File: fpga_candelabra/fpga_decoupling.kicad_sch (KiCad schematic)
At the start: 57 parts

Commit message: fpga_candelabra: more bugfixes & improvements for rev 0.2.0
- Add Digilent JTAG-SMT2-NC onboard
- Add fan controller & 4pin fan header
- Use 9pin header for USB2.0
- Misc fixes for structure

Signed-off-by: Yichuan Gao <gaoyichuan000@gmail.com>
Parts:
- C148, C149, C150, C151, C152, C153, C154, C155, C156, C157, C158: footprint Capacitor_SMD:C_1206_3216Metric -> Capacitor_Tantalum_SMD:CP_EIA-3528-21_Kemet-B; symbol Device:C_Small -> Device:C_Polarized_Small_US; LCSC Part (none) -> C171850
- C159, C166, C167, C168, C169: footprint Capacitor_SMD:C_1210_3225Metric -> Capacitor_Tantalum_SMD:CP_EIA-3528-21_Kemet-B; symbol Device:C_Small -> Device:C_Polarized_Small_US; LCSC Part (none) -> C696807

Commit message: fpga_candelabra: add author & rev to schematics
Signed-off-by: Yichuan Gao <gaoyichuan000@gmail.com>
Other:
- company: (none) -> CHIPS Alliance
- title: (none) -> FPGA Decoupling Capacitors
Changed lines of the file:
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@@
 	(generator_version "8.0")
 	(paper "A4")
+	(title_block
+		(title "FPGA Decoupling Capacitors")
+		(date "2025-02-05")
+		(rev "0.2.0")
+		(company "CHIPS Alliance")
+		(comment 1 "Yichuan Gao")
+		(comment 2 "Yichuan Gao")
+	)
 	(junction
 		(at 171.45 82.55)

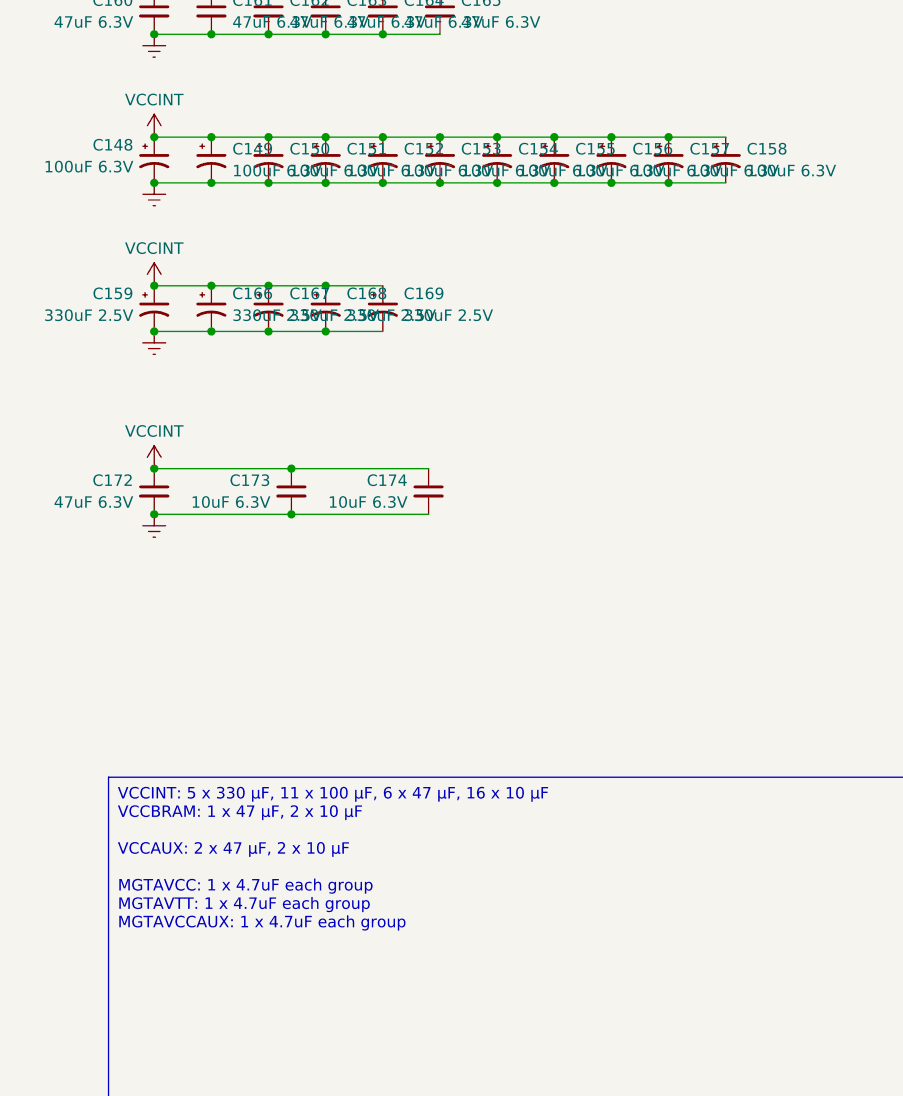
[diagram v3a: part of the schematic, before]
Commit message: fpga_candelabra: update to kicad 9.0
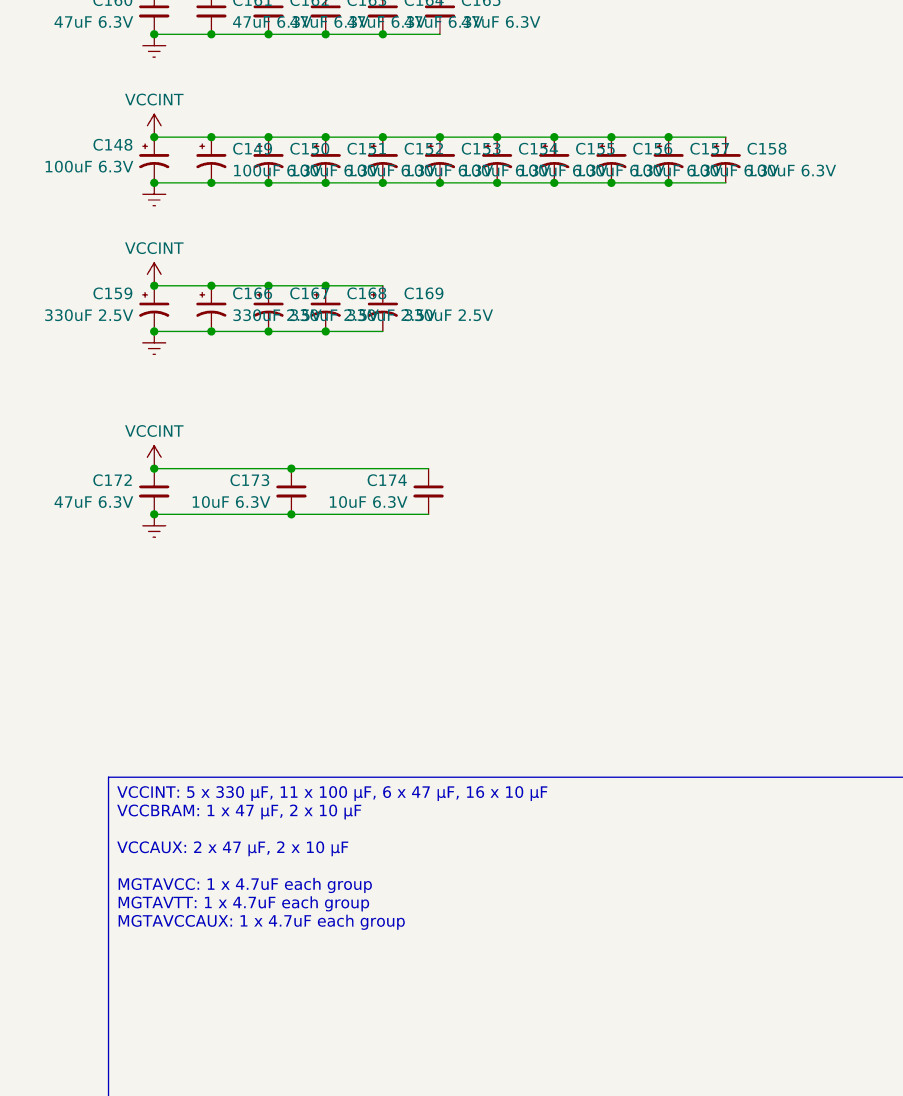
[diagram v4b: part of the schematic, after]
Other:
- company: CHIPS Alliance -> Sipeed
